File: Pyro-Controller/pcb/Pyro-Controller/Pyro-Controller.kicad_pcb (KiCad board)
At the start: 2 copper layers, 27.1 x 21.2 mm, 7 parts, among them J1 Screw_Terminal_01x02, J2 Conn_01x03_Socket, Q1 SiS454DN

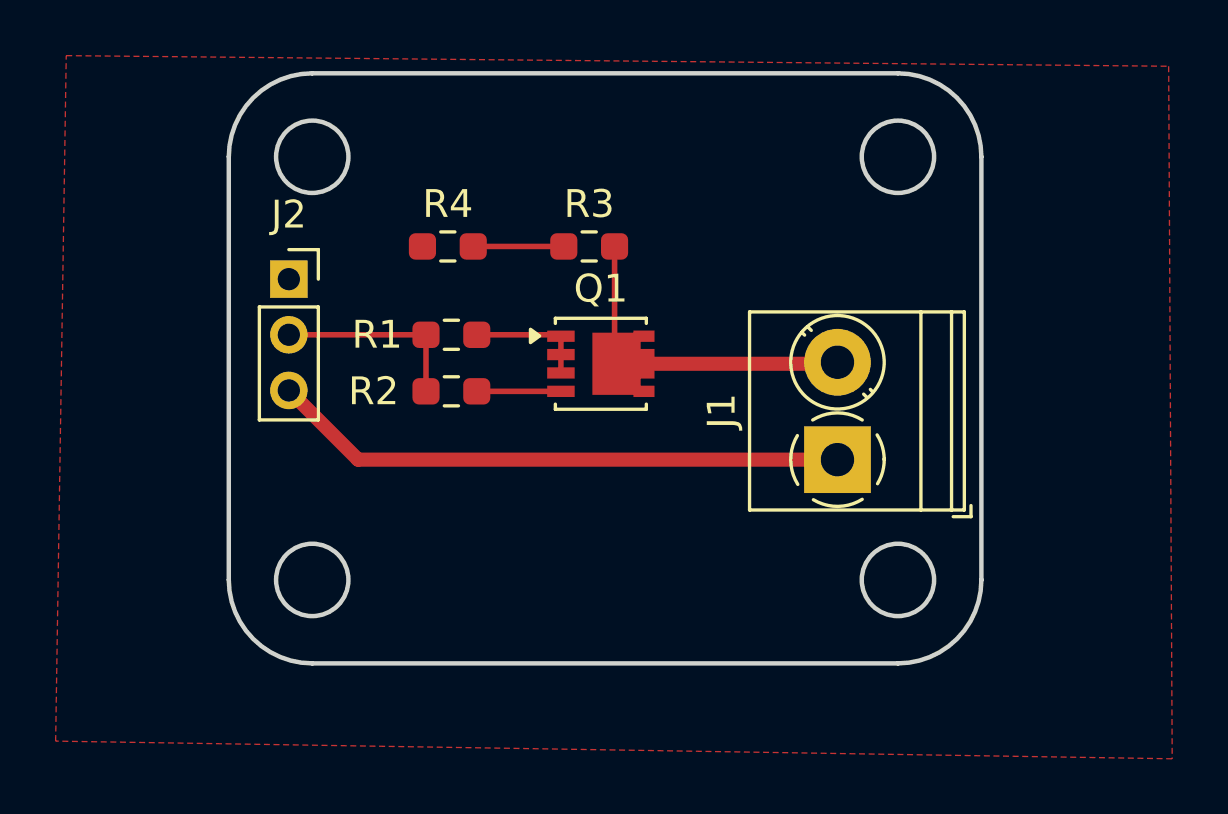
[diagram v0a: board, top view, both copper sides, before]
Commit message: Added testpoint to Pyro Controller
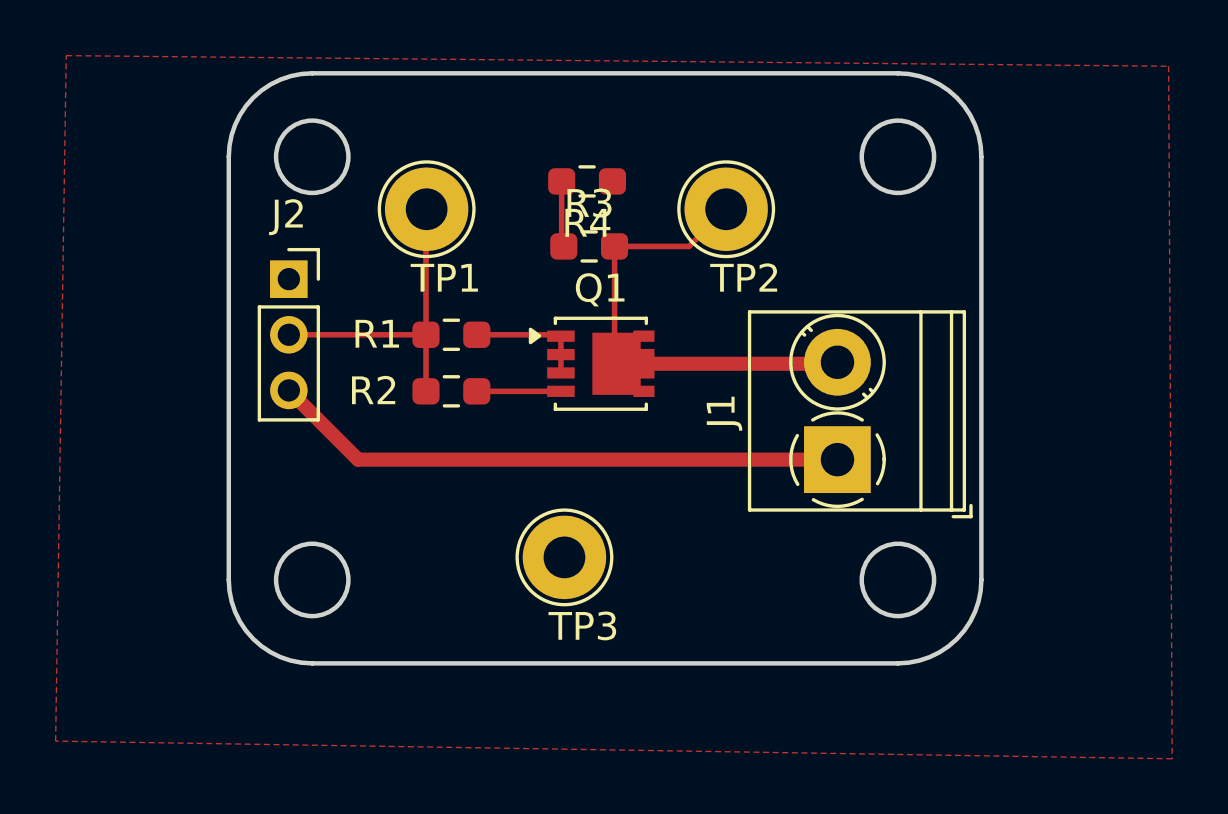
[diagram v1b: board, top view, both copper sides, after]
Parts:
- added TP1: TestPoint, TestPoint:TestPoint_Loop_D2.54mm_Drill1.5mm_Beaded, F.Cu at (30.7, 28.0)
- added TP2: TestPoint, TestPoint:TestPoint_Loop_D2.54mm_Drill1.5mm_Beaded, F.Cu at (41.5, 28.0)
- added TP3: TestPoint, TestPoint:TestPoint_Loop_D2.54mm_Drill1.5mm_Beaded, F.Cu at (35.7, 40.5)
- moved R4 5.52 mm to (36.5, 27.0), turned to 180 degrees
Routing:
- net /PyroController/Input: track 6.98 -> 11.6 mm
- net /PyroController/Output: track 12.2 -> 16.8 mm
- net Net-(R3-Pad2): track 3.26 -> 2.37 mm
